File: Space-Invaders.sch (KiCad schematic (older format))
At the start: 83 parts, among them Q1 BS170, Q2 BS170, Q3 BS170, Q4 BS170, U1 LM556, U2 LM3900, U3 4070, U4 CD4006, U5 LM358, U6 LM386, U7 SN76477, U8 LM3900

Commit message: added switch
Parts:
- added SW?: SW_SPST, symbol Switch:SW_SPST
- R42: value 120k -> 150k
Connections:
- net GND: now also SW?.1 (A)
- net at U7.9 (ENABLE): now also SW?.2 (B)
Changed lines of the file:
@@
 P 3100 5050
 F 0 "R42" H 3050 5125 28  0000 R CNN
-F 1 "120k" H 3175 5125 28  0000 R CNN
+F 1 "150k" H 3175 5125 28  0000 R CNN
 F 2 "" H 3100 4950 50  0001 C CNN
 F 3 "" H 3100 4950 50  0001 C CNN
@@
 	1    0    0    -1
 $EndComp
+$Comp
+L Switch:SW_SPST SW?
+U 1 1 636EF2F6
+P 3150 7675
+F 0 "SW?" V 3196 7587 50  0000 R CNN
+F 1 "SW_SPST" V 3105 7587 50  0000 R CNN
+F 2 "" H 3150 7675 50  0001 C CNN
+F 3 "~" H 3150 7675 50  0001 C CNN
+	1    3150 7675
+	0    -1   -1   0
+$EndComp
+Wire Wire Line
+	3150 6950 3150 7475
+$Comp
+L power:GND #PWR?
+U 1 1 636F6F8B
+P 3150 7875
+F 0 "#PWR?" H 3150 7625 50  0001 C CNN
+F 1 "GND" H 3155 7702 50  0000 C CNN
+F 2 "" H 3150 7875 50  0001 C CNN
+F 3 "" H 3150 7875 50  0001 C CNN
+	1    3150 7875
+	1    0    0    -1
+$EndComp

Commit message: added attack
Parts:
- added C17, C18, C19: 1uF, symbol Xenir:Capacitor
- added C20: .22uF, symbol Xenir:Capacitor
- added R48: 1M, symbol Xenir:Resistor
- added R49, R50: 330k, symbol Xenir:Resistor
- added R51, R53: 150k, symbol Xenir:Resistor
- added R52: 3.9k, symbol Xenir:Resistor
- added R54, R56: 47k, symbol Xenir:Resistor
- added R55: 4.7k, symbol Xenir:Resistor
- added SW2: SW_SPST, symbol Switch:SW_SPST
- added U9: SN76477, symbol Xenir:SN76477
- gave numbers to parts that had none: 1
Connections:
- net +5V: now also U9.1 (ENVSEL1), U9.15 (VREG), U9.19 (PITCH), U9.22 (VCOSEL)
- net GND: now also C17.1, C18.2, C19.1, C20.1, R48.2, R49.1, R50.1, R51.2, R52.2, R53.1, R55.1, SW2.1 (A), U9.2 (GND), U9.25 (MIXSELA), U9.26 (MIXSELB), U9.27 (MIXSELC), U9.28 (ENVSEL2)
- net OUTPUT: now also R56.2
- new net: R50.2, U9.10 (ATTACKR)
- new net: R53.2, U9.11 (AMPR)
- new net: R54.2, U9.12 (FEEDBACKR)
- new net: R54.1, R55.2, R56.1, U9.13 (OUTPUT)
- new net: C20.2, U9.17 (VCOC)
- new net: R52.1, U9.18 (VCOR)
- new net: R51.1, U9.20 (SLFR)
- new net: C19.2, U9.21 (SLFC)
- new net: C17.2, U9.23 (ONESHOTC)
- new net: R48.1, U9.24 (ONESHOTR)
- new net: R49.2, U9.7 (DECAYR)
- new net: C18.1, U9.8 (DECAYCAP)
- new net: SW2.2 (B), U9.9 (ENABLE)
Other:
- note added: "UFO"
- note added: "UFO with\nAttack/Decay"
- moved on the sheet: C15, C16, R42, R43, R44, R45, R46, R47, SW1, U7

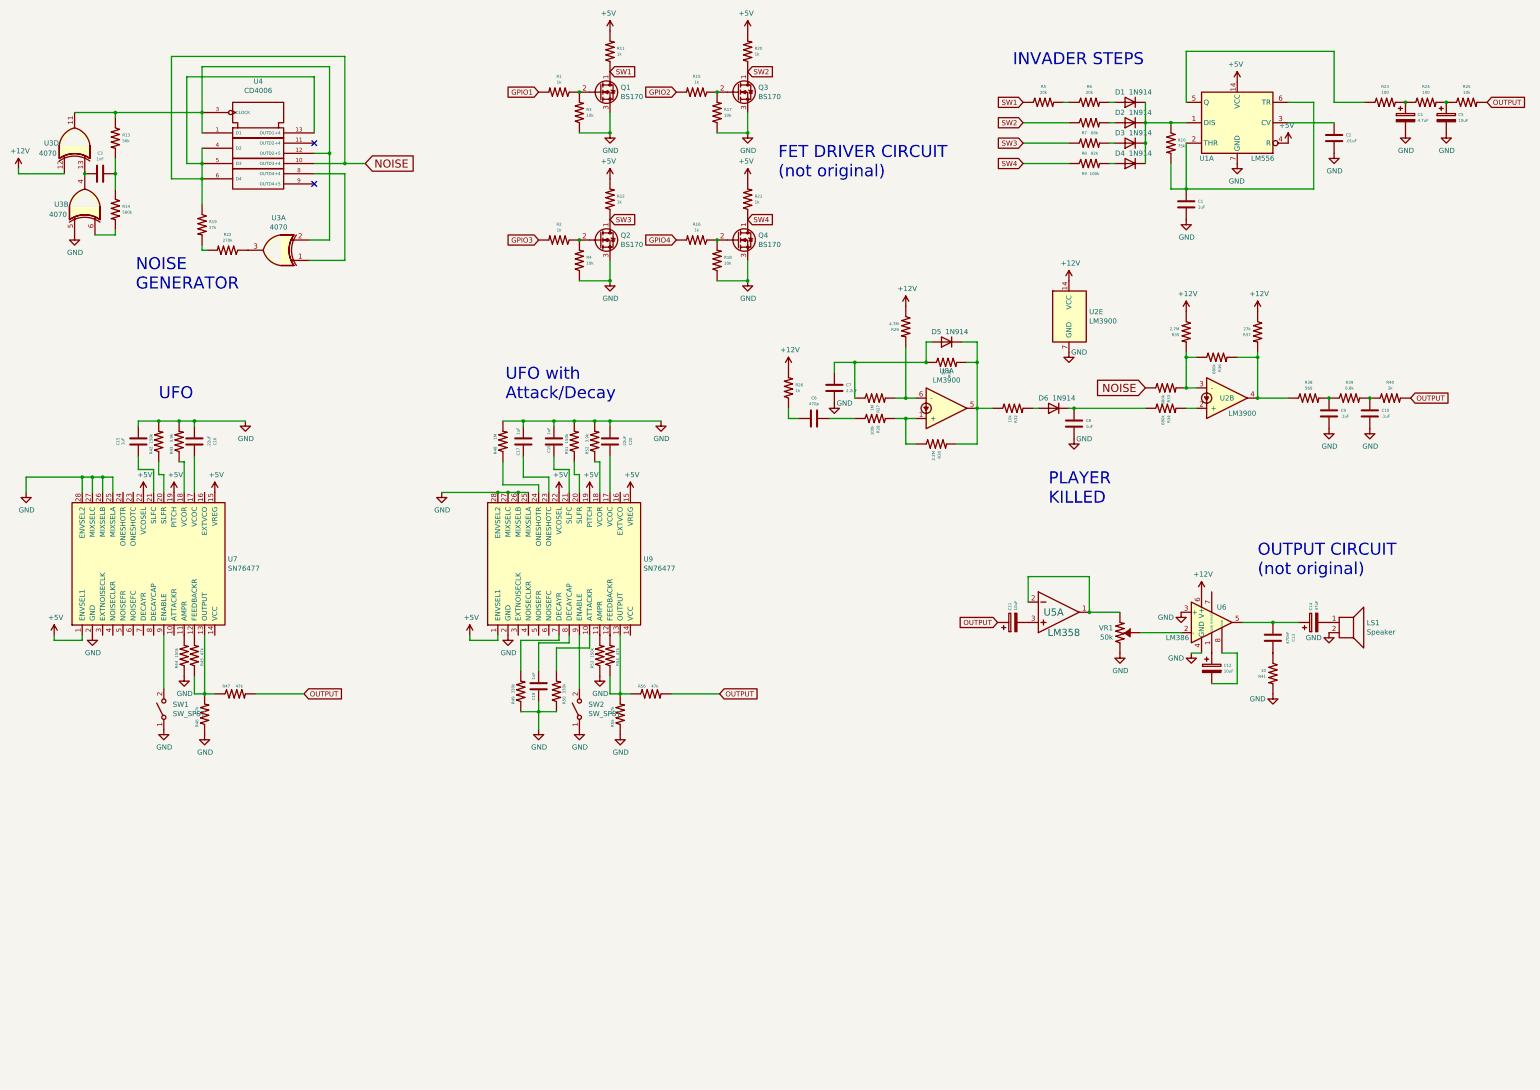
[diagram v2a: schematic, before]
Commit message: added explosion
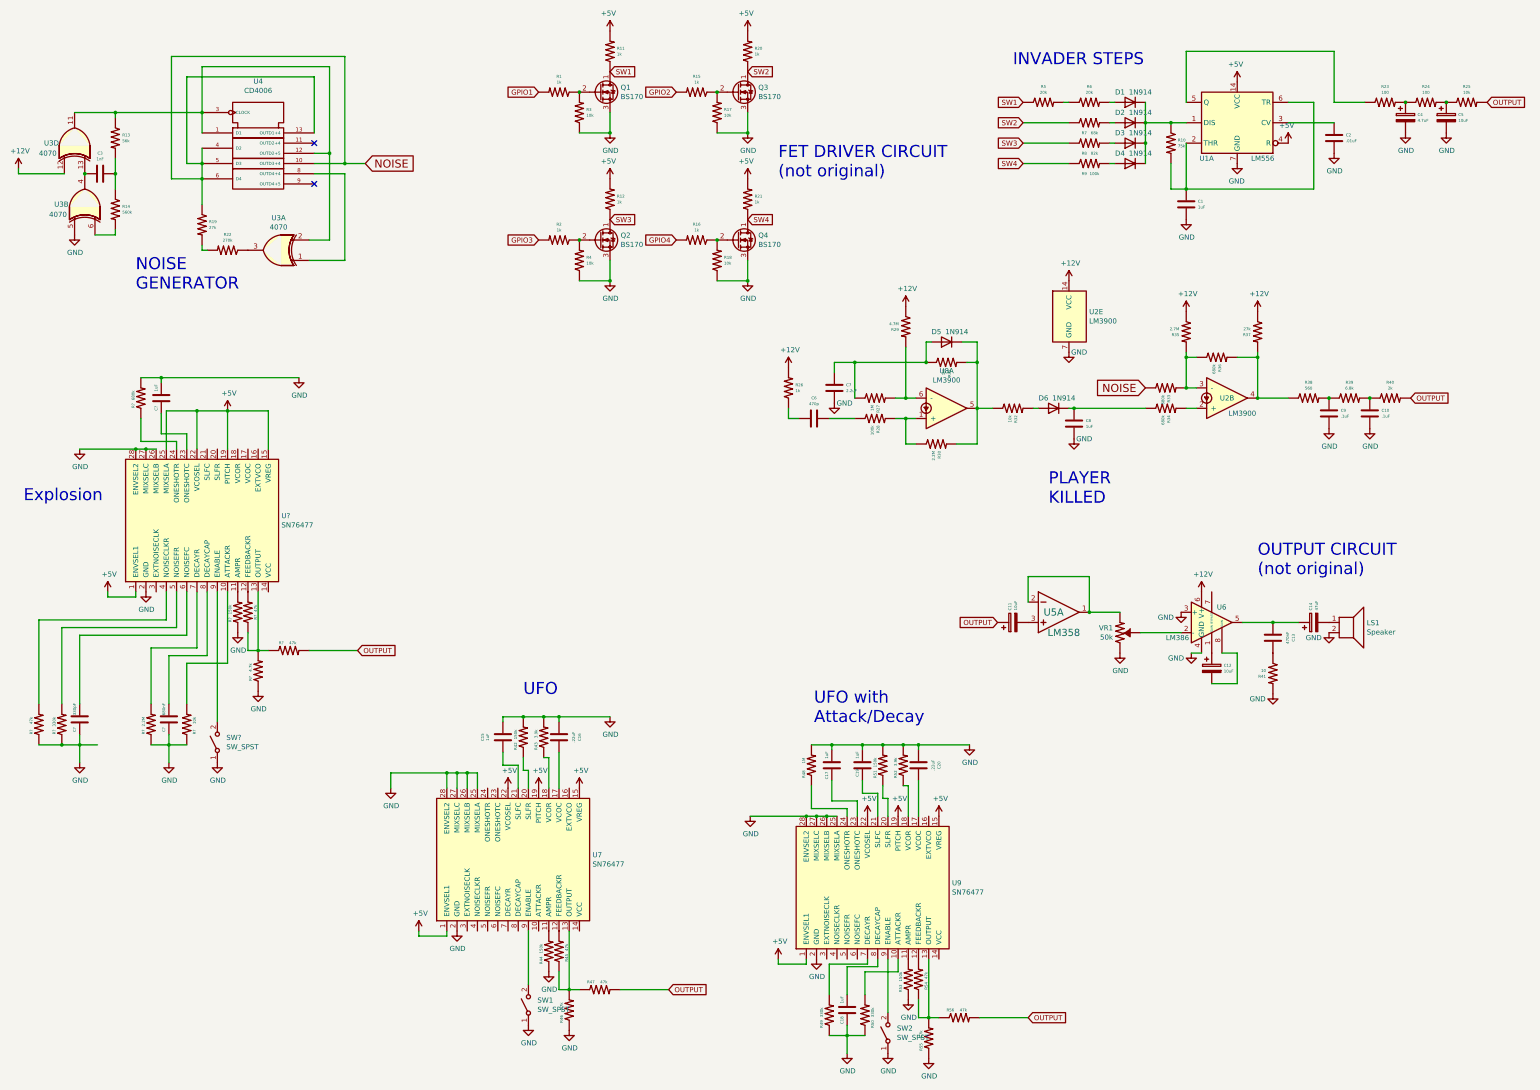
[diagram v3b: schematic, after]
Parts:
- added C?: 1uF, symbol Xenir:Capacitor
- added C?: 680nF, symbol Xenir:Capacitor
- added C?: 330pF, symbol Xenir:Capacitor
- added R?: 4.7k, symbol Xenir:Resistor
- added R? (x3): 47k, symbol Xenir:Resistor
- added R?: 150k, symbol Xenir:Resistor
- added R?: 680k, symbol Xenir:Resistor
- added R?: 2.2M, symbol Xenir:Resistor
- added R?: 10k, symbol Xenir:Resistor
- added R?: 330k, symbol Xenir:Resistor
- added SW?: SW_SPST, symbol Switch:SW_SPST
- added U?: SN76477, symbol Xenir:SN76477
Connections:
- net +5V: now also U?.1 (ENVSEL1), U?.15 (VREG), U?.19 (PITCH), U?.22 (VCOSEL), U?.25 (MIXSELA)
- net GND: now also C?.1, C?.2, C?.2, R?.1, R?.1, R?.1, R?.1, R?.1, R?.1, R?.2, SW?.1 (A), U?.2 (GND), U?.26 (MIXSELB), U?.27 (MIXSELC), U?.28 (ENVSEL2)
- net OUTPUT: now also R?.2
- new net: R?.2, U?.10 (ATTACKR)
- new net: R?.2, U?.11 (AMPR)
- new net: R?.2, U?.12 (FEEDBACKR)
- new net: R?.1, R?.1, R?.2, U?.13 (OUTPUT)
- new net: C?.2, U?.23 (ONESHOTC)
- new net: R?.1, U?.24 (ONESHOTR)
- new net: R?.2, U?.4 (NOISECLKR)
- new net: R?.2, U?.5 (NOISEFR)
- new net: C?.1, U?.6 (NOISEFC)
- new net: R?.2, U?.7 (DECAYR)
- new net: C?.1, U?.8 (DECAYCAP)
- new net: SW?.2 (B), U?.9 (ENABLE)
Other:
- note added: "Explosion"
- moved on the sheet: C15, C16, C17, C18, C19, C20, R42, R43, R44, R45, R46, R47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

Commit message: gg
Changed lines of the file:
@@
 Wire Wire Line
 	1750 7650 1750 7825
-Wire Wire Line
-	1925 7650 1750 7650
 $Comp
 L Xenir:Resistor R?
